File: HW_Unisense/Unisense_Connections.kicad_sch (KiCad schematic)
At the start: 38 parts, among them J2 SW1, J3 RS485, J3 SW2, J4 GeigerCounter, J5 OneWire, J5 WS2812, J6 LED1, J7 LED2, J8 LED3, P1 SM02B-NSHSS-TB(LF)(SN), Q1 BSN20, Q2 BSN20, Q4 BSN20, Q5 AO3400A, Q6 AO3400A, Q7 AO3400A, SW3 K2-1102SP-C4SC-04, SW4 K2-1102SP-C4SC-04, U2 S4B-PH-SM4-K-TB(LF)(SN)

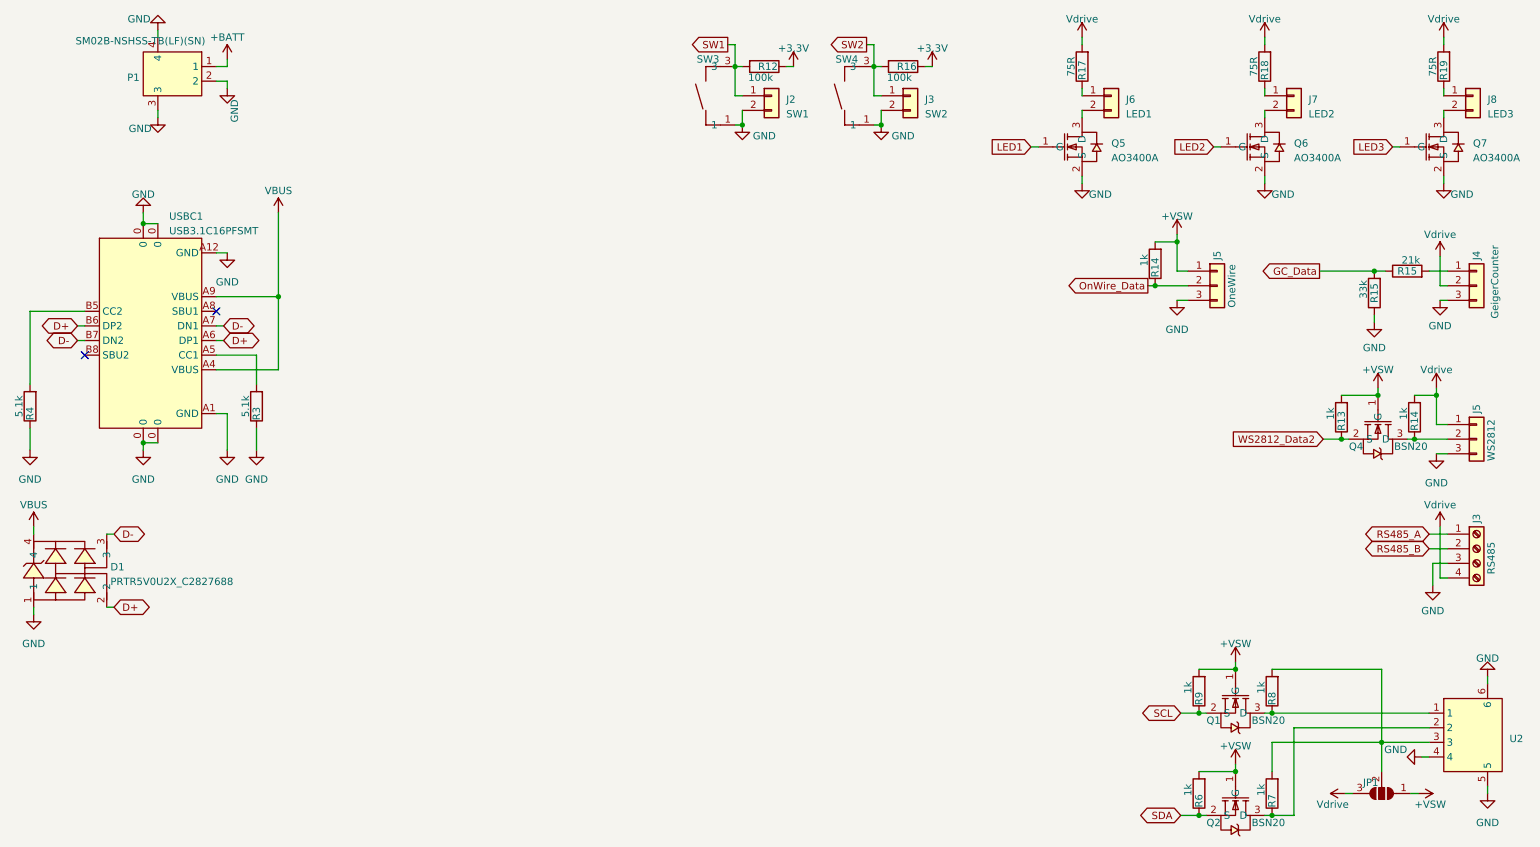
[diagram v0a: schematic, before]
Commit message: change power net names, as V8 handles them like a champ
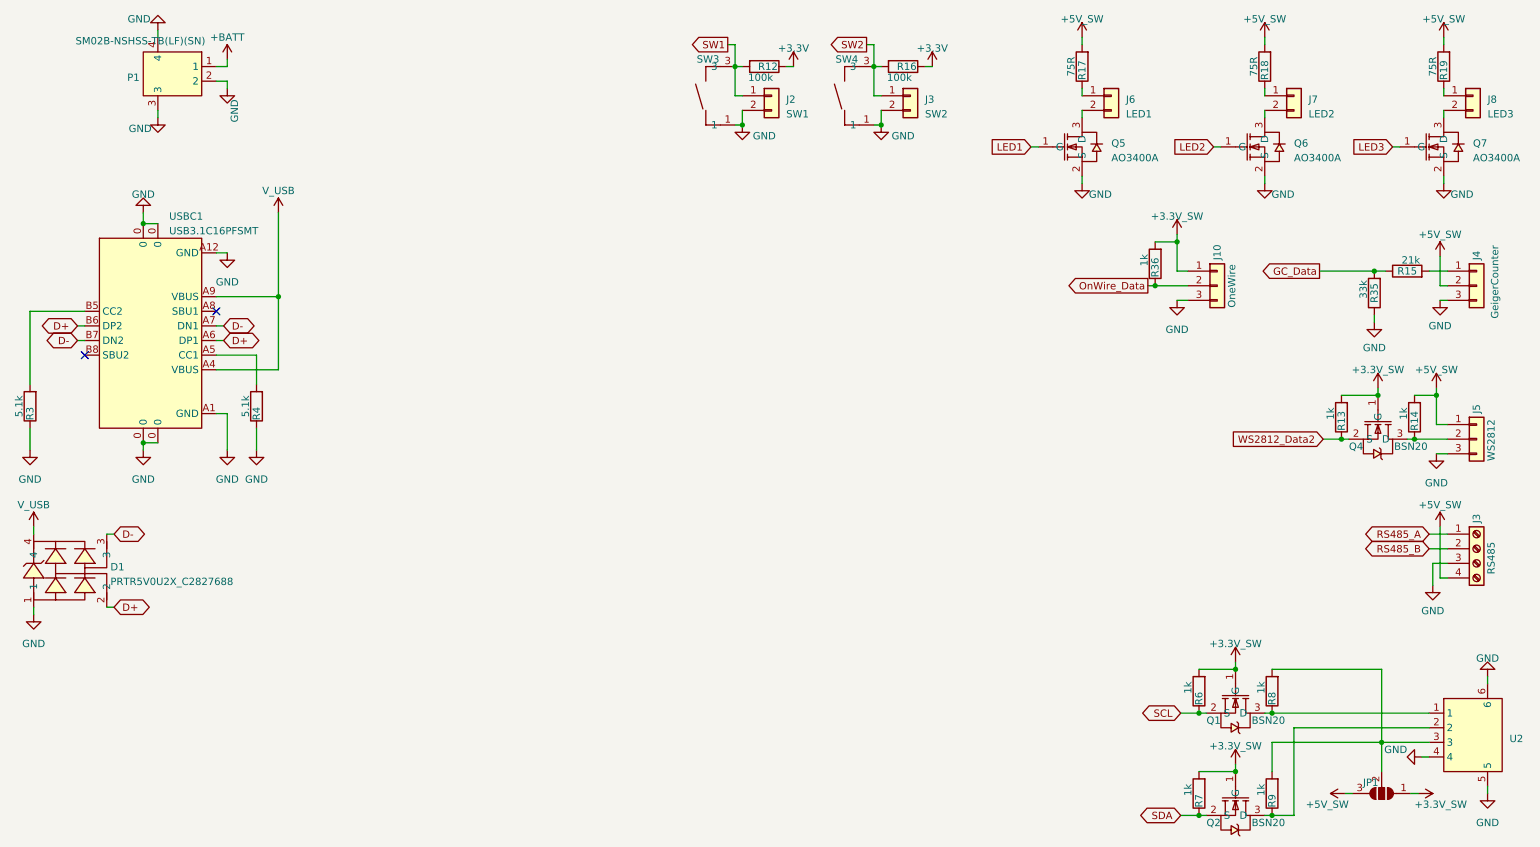
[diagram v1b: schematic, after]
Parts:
- renumbered J5 to J10, R4 to R3, R15 to R35, R14 to R36, R3 to R4, R9 to R6, R6 to R7, R7 to R9
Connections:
- net +VSW renamed +3.3V_SW
- net VBUS renamed V_USB
- net Vdrive renamed +5V_SW

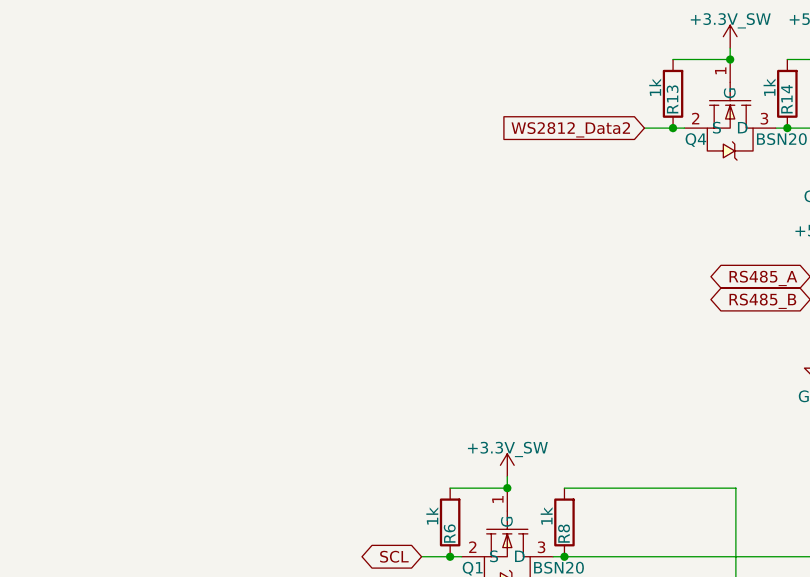
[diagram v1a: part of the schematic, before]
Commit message: add mor sensors, place parts
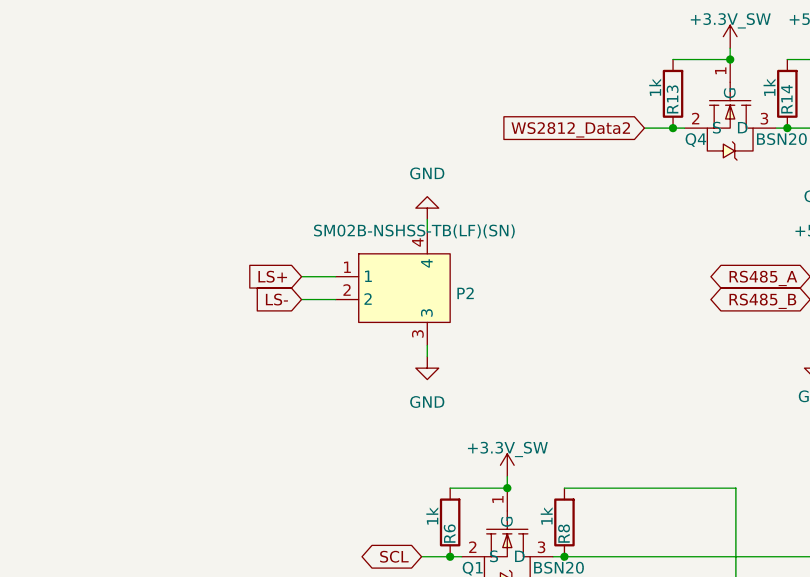
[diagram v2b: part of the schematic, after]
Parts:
- added P2: SM02B-NSHSS-TB(LF)(SN), burgerLibFP:CONN-SMD_SM02B-NSHSS-TB-LF-SN, symbol burgerLib:SM02B-NSHSS-TB(LF)(SN)
- JP1: footprint (none) -> Jumper:SolderJumper-3_P1.3mm_Open_Pad1.0x1.5mm
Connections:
- net GND: now also P2.3, P2.4
- new net LS+: P2.1
- new net LS-: P2.2
